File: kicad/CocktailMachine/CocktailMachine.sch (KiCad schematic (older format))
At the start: 27 parts

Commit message: Draft 1: Missing footprints
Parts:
- added POT?: P120PK-Y25BR10K, digikey-footprints:Potentiometer_P120PK-Y25BR10K, symbol dk_Rotary-Potentiometers-Rheostats:P120PK-Y25BR10K
- added U? (x2): TXB0104PWR, digikey-footprints:TSSOP-14_W4.4mm, symbol dk_Logic-Translators-Level-Shifters:TXB0104PWR
- R1: value R_US -> 220
- R2: value R_US -> 220k
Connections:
- net +3V3: now also U?.1 (VCCA), U?.1 (VCCA), U?.8 (OE), U?.8 (OE)
- net +5V: now also LCD?.15 (LED+), LCD?.2 (VDD), POT?.1 (CCW), U?.14 (VCCB), U?.14 (VCCB)
- net GND: now also LCD?.1 (VSS), LCD?.16 (LED-), POT?.3 (CW), U?.7 (GND), U?.7 (GND)
- net MCU_EN: now reaches U?.17 (SHD/SD2)
- net MCU_EN: now also U?.4 (A3)
- net MCU_DB7: now reaches U?.18 (SWP/SD3)
- net MCU_DB7: now also U?.5 (A4)
- net MCU_DB5: now reaches U?.19 (SCS/CMD)
- net MCU_DB6: now reaches U?.20 (SCK/CLK)
- net MCU_RS: now reaches U?.21 (SDO/SD0)
- net MCU_RS: now also U?.2 (A1)
- net MCU_RW: now reaches U?.22 (SDI/SD1)
- net MCU_RW: now also U?.3 (A2)
- net MCU_DB4: now reaches U?.25 (IO0)
- net LCD_DB4: now reaches LCD?.11 (DB4)
- net LCD_DB4: now also U?.11 (B3)
- net LCD_DB5: now reaches LCD?.12 (DB5)
- net LCD_DB5: now also U?.12 (B2)
- net LCD_DB6: now reaches LCD?.13 (DB6)
- net LCD_DB6: now also U?.13 (B1)
- net LCD_DB7: now reaches LCD?.14 (DB7)
- net LCD_DB7: now also U?.10 (B4)
- net V0_DISPLAY_CONTRAST: now reaches LCD?.3 (V0)
- net LCD_RS: now reaches LCD?.4 (RS)
- net LCD_RS: now also U?.13 (B1)
- net LCD_RW: now reaches LCD?.5 (R/W)
- net LCD_RW: now also U?.12 (B2)
- net LCD_EN: now reaches LCD?.6 (En)
- net LCD_EN: now also U?.11 (B3)
- no-connect marks 1 -> 8
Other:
- note added: "3.3V to 5V Level Shifter"
- note added: "Potentiometer Display Brightness\n"
- moved on the sheet: C?, J?, LCD?, R1, R2, S?, U?A

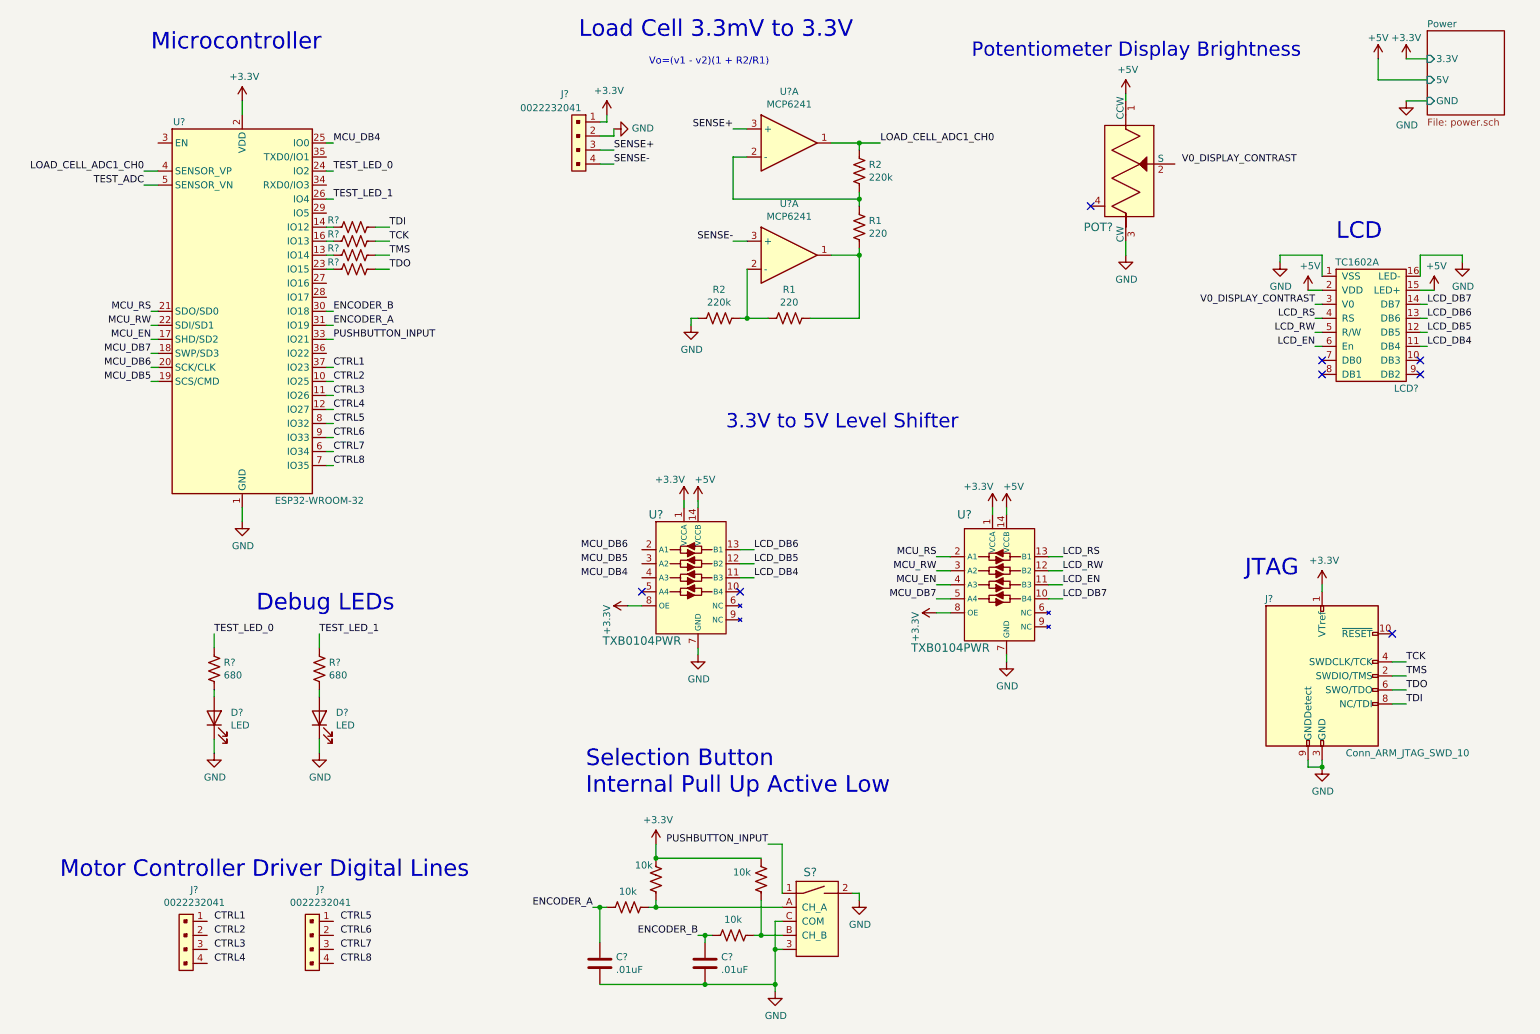
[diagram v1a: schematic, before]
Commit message: - Add decoupling for all ICs - Separate power planes from buck for noise reduction - Miscellaneous fixes
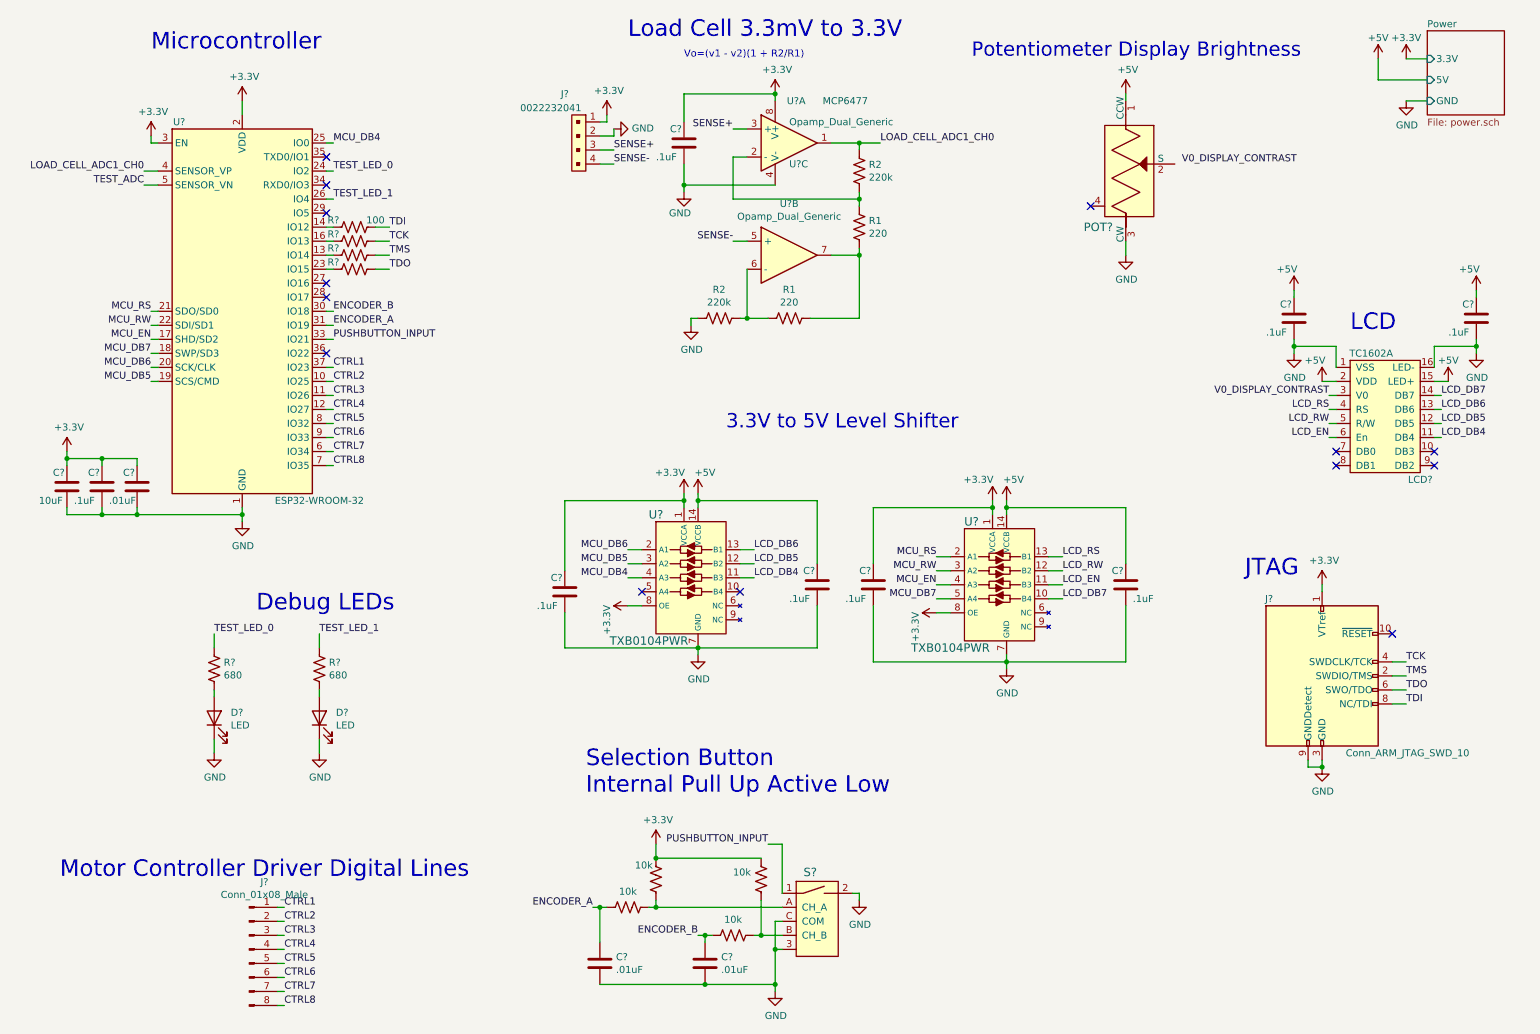
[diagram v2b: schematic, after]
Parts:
- removed J? (x2): 0022232041, digikey-footprints:PinHeader_1x4_P2.54mm_Drill1.02mm, symbol dk_Rectangular-Connectors-Headers-Male-Pins:0022232041
- removed U?: MCP6241, symbol Device:Opamp_Dual_Generic
- added C?: .01uF, symbol Device:C
- added C? (x8): .1uF, symbol Device:C
- added C?: 10uF, symbol Device:C
- added J?: Conn_01x08_Male, symbol Connector:Conn_01x08_Male
- added U? (x2): Opamp_Dual_Generic, symbol Device:Opamp_Dual_Generic
- R1, R2, R? (x6): footprint (none) -> Resistor_THT:R_Axial_DIN0204_L3.6mm_D1.6mm_P2.54mm_Vertical
- U?: value MCP6241 -> MCP6477
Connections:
- net +3V3: now also U?.3 (EN), C?.1, C?.1, C?.1, C?.1, C?.1, C?.1, U?.8 (V+)
- net +5V: now also C?.1, C?.1, C?.1, C?.1
- net CTRL1: now also J?.1 (Pin_1)
- net CTRL2: now also J?.2 (Pin_2)
- net CTRL3: now also J?.3 (Pin_3)
- net CTRL4: now also J?.4 (Pin_4)
- net CTRL5: now also J?.5 (Pin_5)
- net CTRL6: now also J?.6 (Pin_6)
- net CTRL7: now also J?.7 (Pin_7)
- net CTRL8: now also J?.8 (Pin_8)
- net GND: now also C?.2, C?.2, C?.2, C?.2, C?.2, C?.2, C?.2, C?.2, C?.2, C?.2, U?.4 (V-)
- net MCU_DB4: now also U?.4 (A3)
- net MCU_DB5: now also U?.3 (A2)
- net MCU_DB6: now also U?.2 (A1)
- net SENSE-: now also U?.5 (+)
- net at R1.1, R1.2: now also U?.7
- net at R1.2, R2.1: now also U?.6 (-)
- no-connect marks 8 -> 14
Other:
- moved on the sheet: LCD?
